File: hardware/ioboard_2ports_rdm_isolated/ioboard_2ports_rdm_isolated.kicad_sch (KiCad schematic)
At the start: 30 parts

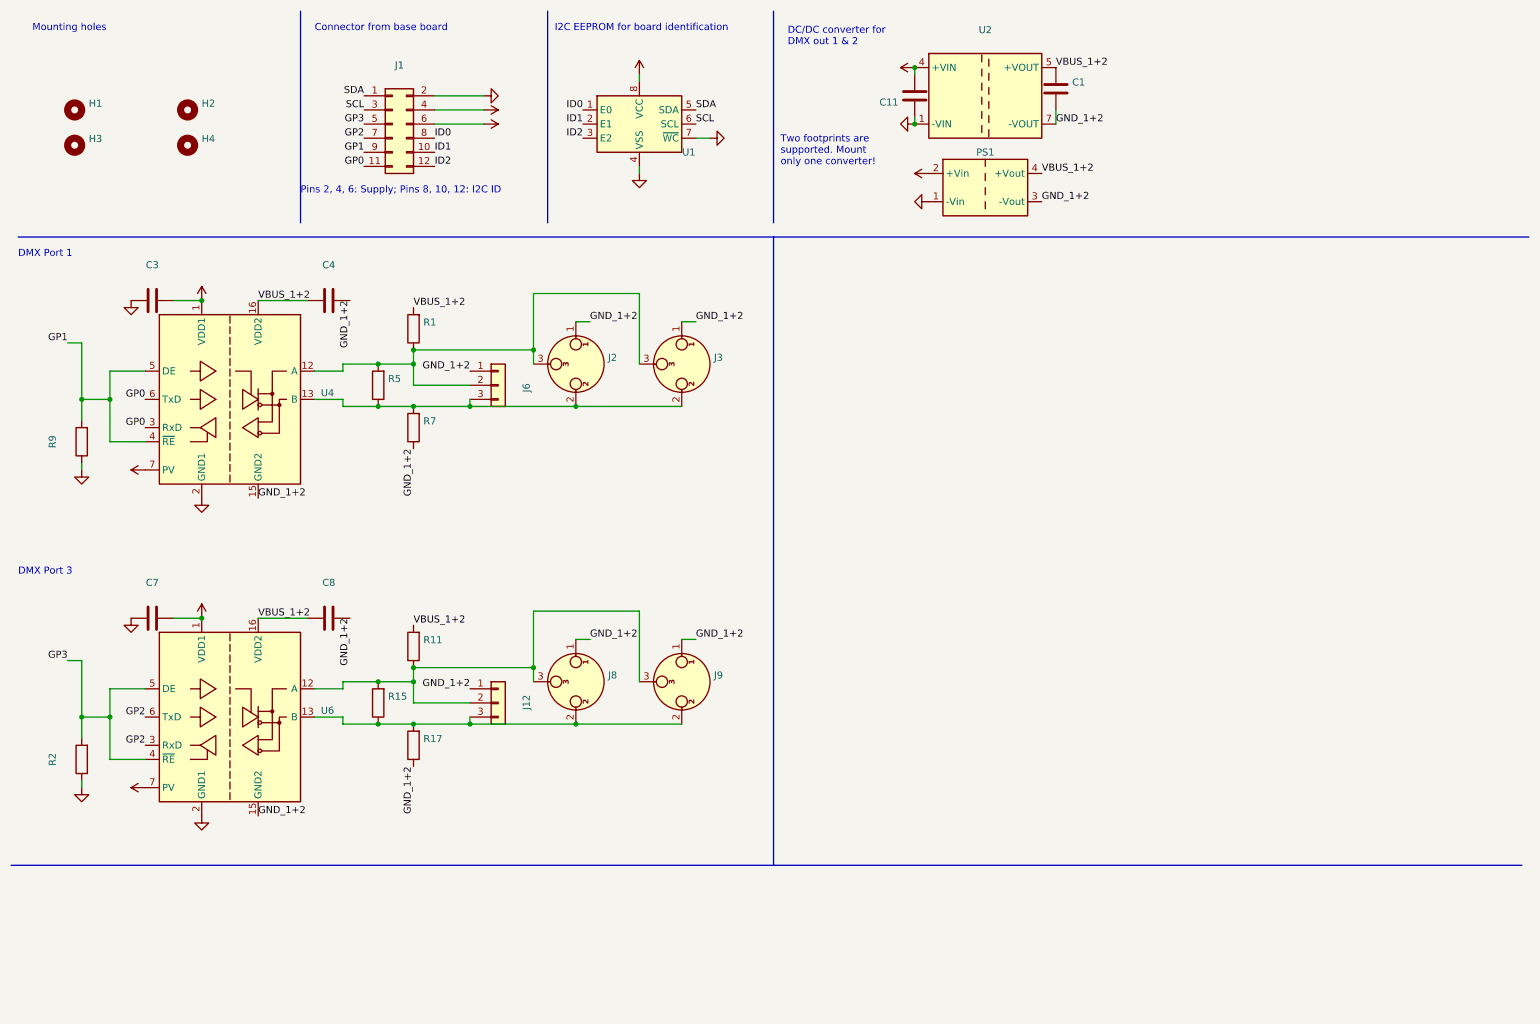
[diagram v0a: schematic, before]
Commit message: Fix gitignore Move NC3FD-H.pretty footprint library to a common location and update references Rework ioboard_2ports_rdm_isolated
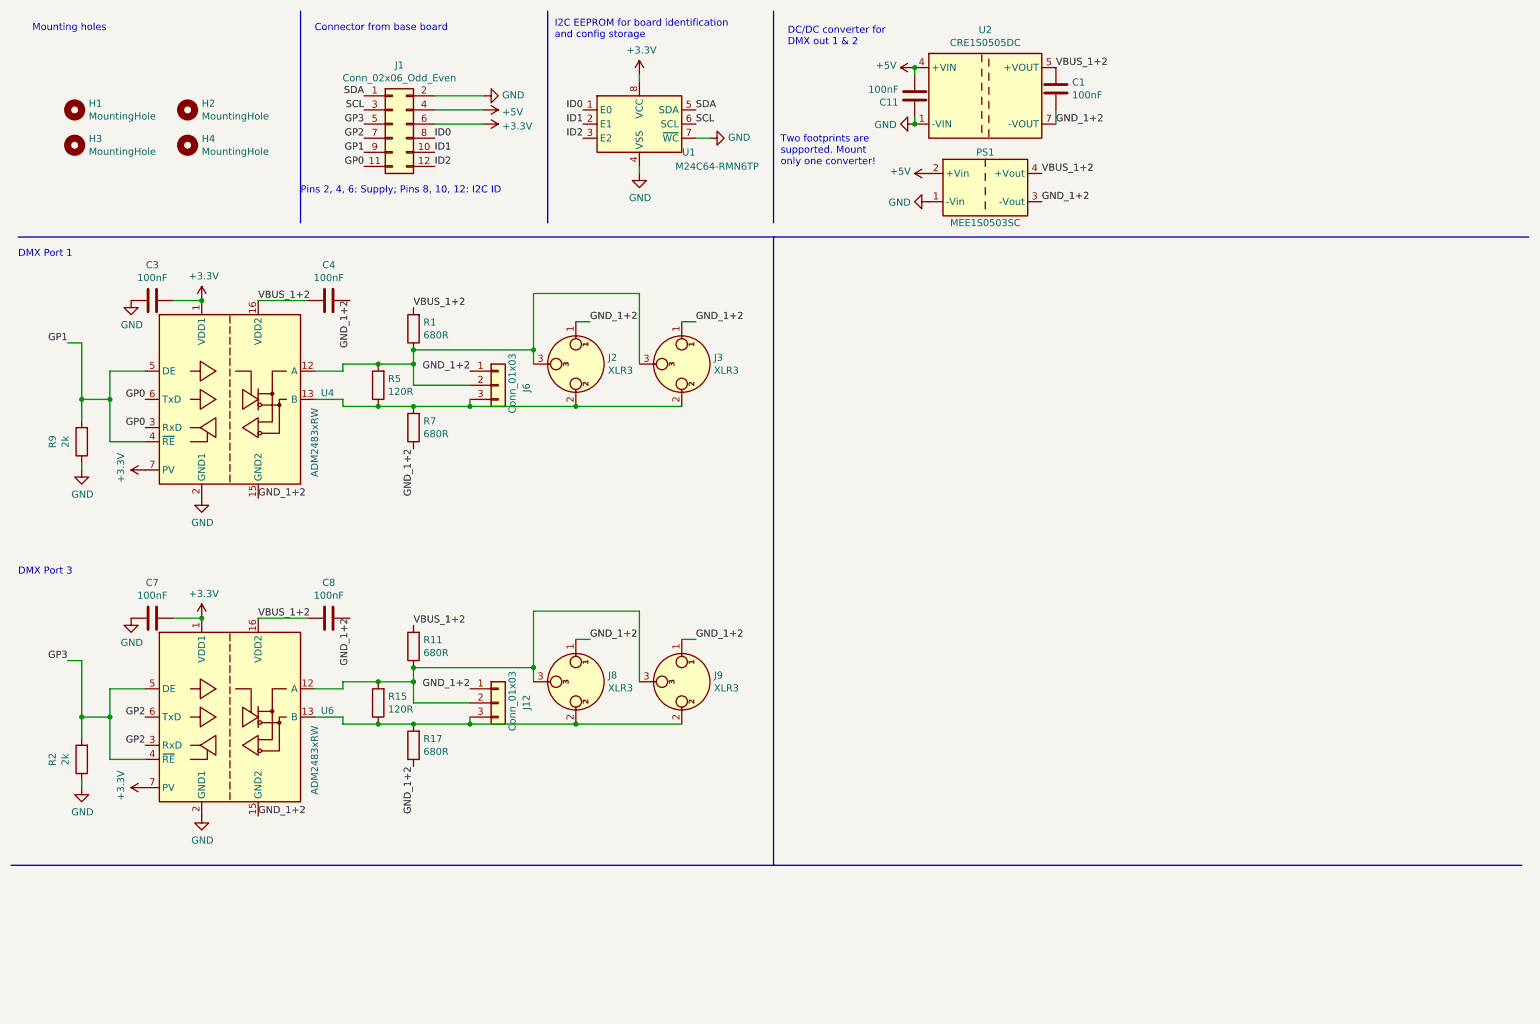
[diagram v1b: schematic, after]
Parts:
- C1, C11, C3, C4, C7, C8: value (none) -> 100nF; footprint (none) -> Capacitor_SMD:C_0603_1608Metric
- H1, H2, H3, H4: value (none) -> MountingHole; footprint (none) -> MountingHole:MountingHole_3.2mm_M3
- J1: value (none) -> Conn_02x06_Odd_Even; footprint (none) -> Connector_PinHeader_2.54mm:PinHeader_2x06_P2.54mm_Vertical
- J12, J6: value (none) -> Conn_01x03; footprint (none) -> Connector_PinHeader_2.54mm:PinHeader_1x03_P2.54mm_Vertical
- J2, J8: value (none) -> XLR3; footprint (none) -> Connector_Audio:Jack_XLR_Neutrik_NC3FAAH_Horizontal
- J3, J9: value (none) -> XLR3; footprint (none) -> NC3FD-H:Jack_XLR_Neutrik_NC3FD-H_Horizontal
- PS1: value (none) -> MEE1S0503SC; footprint (none) -> Converter_DCDC:Converter_DCDC_muRata_CRE1xxxxxx3C_THT
- R1, R11, R17, R7: value (none) -> 680R; footprint (none) -> Resistor_SMD:R_0603_1608Metric_Pad0.98x0.95mm_HandSolder
- R15, R5: value (none) -> 120R; footprint (none) -> Resistor_SMD:R_0603_1608Metric_Pad0.98x0.95mm_HandSolder
- R2, R9: value (none) -> 2k; footprint (none) -> Resistor_SMD:R_0805_2012Metric_Pad1.20x1.40mm_HandSolder
- U1: value (none) -> M24C64-RMN6TP; footprint (none) -> Package_SO:SOIC-8_3.9x4.9mm_P1.27mm
- U2: value (none) -> CRE1S0505DC; footprint (none) -> Converter_DCDC:Converter_DCDC_muRata_CRE1xxxxxxDC_THT
- U4, U6: value (none) -> ADM2483xRW; footprint (none) -> Package_SO:SOIC-16W_7.5x10.3mm_P1.27mm
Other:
- note added: "I2C EEPROM for board identification and config storage"
- note removed: "I2C EEPROM for board identification"
